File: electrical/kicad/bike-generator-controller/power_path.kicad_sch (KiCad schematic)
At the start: 0 parts

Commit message: feat: build provisional power path schematic
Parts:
- added F1: 20A DC / PROVISOIRE, symbol Device:Fuse
- added F2: F_AUX / PROVISOIRE, symbol Device:Fuse
- added J4: RECTIFIER_IN / PROVISOIRE, symbol Connector_Generic:Conn_01x02
- added J5: BUCK_400W_IN / PROVISOIRE, symbol Connector_Generic:Conn_01x02
- added R7: 2mR 4T / PROVISOIRE, symbol Device:R_Shunt
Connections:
- new net: F1.2, R7.1
- new net: F1.1, J4.1 (Pin_1)
- new net AUX_IN_PROTECTED: F2.2
- new net BUS_PROTECTED: F2.1, J5.1 (Pin_1), R7.4
- new net GND: J4.2 (Pin_2), J5.2 (Pin_2)
- new net SHUNT_HI_K: R7.2
- new net SHUNT_LO_K: R7.3
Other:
- note added: "CHEMIN DE PUISSANCE 400 W - composants mecaniques a confirmer"
- note added: "Depart auxiliaire protege vers LM5164 (10-60 V vers 5 V)"
- note added: "Protection surtension / TVS : A DIMENSIONNER apres mesures generatrice"

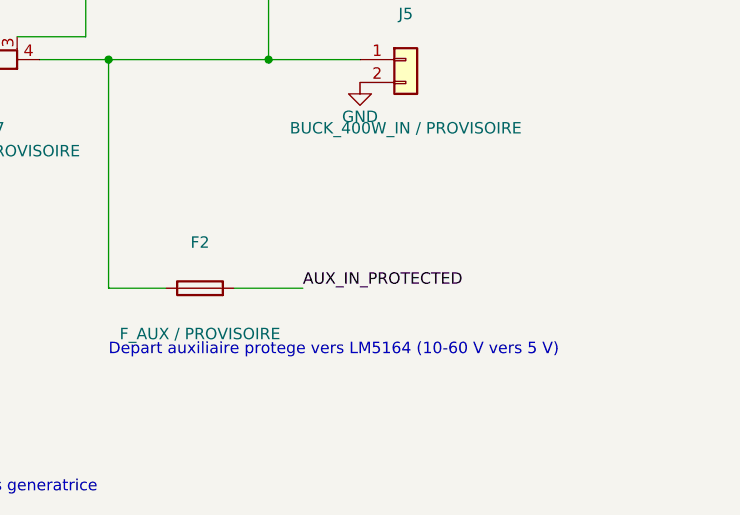
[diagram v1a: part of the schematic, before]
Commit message: feat: add LM5164 auxiliary supply schematic
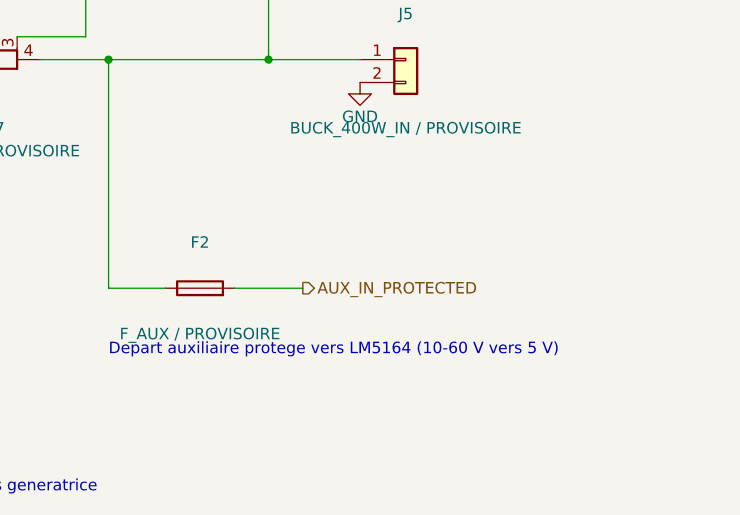
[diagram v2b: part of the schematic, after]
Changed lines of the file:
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@@
-		)
-	)
-	(label "AUX_IN_PROTECTED"
-		(at 143.51 101.6 0)
-		(effects
-			(font
-				(size 1.27 1.27)
-			)
-			(justify left bottom)
 		)
 	)
@@
 		(effects
 			(font
+				(size 1.27 1.27)
+			)
+			(justify left)
+		)
+	)
+	(hierarchical_label "AUX_IN_PROTECTED"
+		(shape output)
+		(at 143.51 101.6 0)
+		(effects
+			(font

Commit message: feat: establish controller PCB V1 design baseline
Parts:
- F1: value 20A DC / PROVISOIRE -> ABC-V-20-R; footprint (none) -> BikeGenerator:Fuse_Eaton_ABC-V-20-R_Axial_P38.10mm; Current Rating (none) -> 20 A; Interrupt Rating (none) -> 10 kA at 125 VDC; MPN (none) -> ABC-V-20-R; Manufacturer (none) -> Eaton Bussmann; Mounting (none) -> Axial THT; Requirement (none) -> Source-specific; 20A maximum; 125VDC minimum; Voltage Rating (none) -> 125 VDC / 250 VAC
- F2: footprint (none) -> BikeGenerator:Fuse_Littelfuse_0449001MR_6.10x2.69mm
- J4: value RECTIFIER_IN / PROVISOIRE -> PHOENIX 1711725 / RECTIFIER_IN; footprint (none) -> TerminalBlock_Phoenix:TerminalBlock_Phoenix_MKDS-3-2-5.08_1x02_P5.08mm_Horizontal; Datasheet Source (none) -> Phoenix Contact official product page; MPN (none) -> 1711725; Manufacturer (none) -> Phoenix Contact; Rated Current (none) -> 24 A; Rated Voltage (none) -> 400 V (III/2); Selection Note (none) -> V1 main-path connector; board path limited to 20 A continuo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; Wire Range (none) -> AWG 24-12 / 0.2-4 mm2 solid
- J5: value BUCK_400W_IN / PROVISOIRE -> PHOENIX 1711725 / BUCK_IN; footprint (none) -> TerminalBlock_Phoenix:TerminalBlock_Phoenix_MKDS-3-2-5.08_1x02_P5.08mm_Horizontal; Datasheet Source (none) -> Phoenix Contact official product page; MPN (none) -> 1711725; Manufacturer (none) -> Phoenix Contact; Rated Current (none) -> 24 A; Rated Voltage (none) -> 400 V (III/2); Selection Note (none) -> V1 main-path connector; board path limited to 20 A continuo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; Wire Range (none) -> AWG 24-12 / 0.2-4 mm2 solid
- R7: value 2mR 4T / PROVISOIRE -> CSS4J-4026K-2L00F 2mR; footprint (none) -> Resistor_SMD:R_Shunt_Isabellenhuette_BVR4026; MPN (none) -> CSS4J-4026K-2L00F; Manufacturer (none) -> Bourns
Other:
- note added: "BUS_PROTECTED : 80 V MAX CONTINU - TVS pour transitoires courts, choix source-specifique"
- note added: "Depart auxiliaire protege vers LM5164 (10-80 V vers 5 V)"
- note removed: "Depart auxiliaire protege vers LM5164 (10-60 V vers 5 V)"
- note removed: "Protection surtension / TVS : A DIMENSIONNER apres mesures generatrice"

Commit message: wip: checkpoint controller routing before review
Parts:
- added D1: SMCJ70A, Diode_SMD:D_SMC, symbol Device:D_Zener
- added D2: DBI25-16A / 3PH BRIDGE, BikeGenerator:Diode_Bridge_Diotec_DBI-A_5Pin_P7.50mm, symbol BikeGenerator:DBI25-16A
- added J8: 3PH_GEN_IN (1=U 2=V 3=W), TerminalBlock_Phoenix:TerminalBlock_Phoenix_MKDS-3-3-5.08_1x03_P5.08mm_Horizontal, symbol Connector_Generic:Conn_01x03
- F1: value ABC-V-20-R -> 0456020.ER / 20A; footprint BikeGenerator:Fuse_Eaton_ABC-V-20-R_Axial_P38.10mm -> BikeGenerator:Fuse_Littelfuse_456_10.08x3.05mm_P9.35mm; Interrupt Rating 10 kA at 125 VDC -> 100 A @125 VAC; 300 A @100 VDC; 500 A @72 VDC; 1000 A @32 V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; MPN ABC-V-20-R -> 0456020.ER; Manufacturer Eaton Bussmann -> Littelfuse; Mounting Axial THT -> SMD; Requirement Source-specific; 20A maximum; 125VDC minimum -> 20 A maximum; voltage and interrupt ratings per Littelfuse 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; Thermal_Management (none) -> Rated-current reference: >=100 um copper and >=10 mm trace 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; Voltage Rating 125 VDC / 250 VAC -> 125 VAC / 100 VDC
- J1: renamed from J4; value PHOENIX 1711725 / RECTIFIER_IN -> DC_GEN_IN / DNP (DC VARIANT); Assembly (none) -> DNP by default - DC generator variant only; Warning (none) -> Respect polarity; never use together with J8
- renumbered J5 to J2, R7 to R1
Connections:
- net BUS_PROTECTED: now also J2.2 (Pin_2), R1.1; no longer J2.1 (Pin_1), R1.4
- net GND: now also J2.1 (Pin_1), D1.2 (A), D2.1 (DC-); no longer J2.2 (Pin_2)
- net SHUNT_HI_K: now also R1.3; no longer R1.2
- net SHUNT_LO_K: now also R1.2; no longer R1.3
- net at F1.2: now also R1.4, D1.1 (K); no longer R1.1
- net RECTIFIED_RAW: now reaches F1.1, J1.1 (Pin_1)
- net RECTIFIED_RAW: now also D2.5 (DC+)
- new net GEN_PHASE_U: D2.4 (AC3), J8.1 (Pin_1)
- new net GEN_PHASE_V: D2.3 (AC2), J8.2 (Pin_2)
- new net GEN_PHASE_W: D2.2 (AC1), J8.3 (Pin_3)
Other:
- note added: "DEFAULT: populate J8 + D2 (3-PHASE INPUT). DC VARIANT: populate J1; D2/J8 may be DNP. ONE INPUT ONLY - NEVER CONNECT J1 AND J8 TO SOURCES AT THE SAME TIME. J1 POLARITY MUST BE RESPECTED."
- note added: "ENTREE GARANTIE <= 70 V CONTINU. SMCJ70A : ecretage transitoire best effort ; INA228 non garantie < 85 V."
- note added: "F1 - THERMIQUE (Littelfuse 0456020.ER) A 20 A : recommandation constructeur >= 100 um Cu et piste >= 10 mm. Si la fabrication differe : valider Tcorps F1 <= 90 degC a Tamb = 25 degC."
- note removed: "BUS_PROTECTED : 80 V MAX CONTINU - TVS pour transitoires courts, choix source-specifique"
- moved on the sheet: F2, J2, R1

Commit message: feat: close controller v1 design and define integrated v2
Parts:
- D2: Thermal Note (none) -> ABOVE 4A USE >=35x25mm ALUMINUM HEATSINK/CHASSIS + TIM + M4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
- F2: value F_AUX / PROVISOIRE -> 0449001.MR / 1A 125V Slo-Blo; MPN (none) -> 0449001.MR; Manufacturer (none) -> Littelfuse
- J1: value DC_GEN_IN / DNP (DC VARIANT) -> DC_GEN_IN / DIRECT DC VARIANT; Assembly DNP by default - DC generator variant only -> Populate on first prototypes - direct DC source variant; Populate (none) -> YES - FIRST PROTOTYPES; Safety Note (none) -> NEVER CONNECT OR ENERGIZE J1 AND J8 AT THE SAME TIME
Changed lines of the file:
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@@
 	(generator_version "10.0")
 	(paper "A4")
+	(text "F1 - THERMIQUE (Littelfuse 0456020.ER)\nA 20 A : recommandation constructeur >= 100 um Cu et piste >= 10 mm.\nSi la fabrication differe : valider Tcorps F1 <= 90 degC a Tamb = 25 degC."
+		(exclude_from_sim no)
+		(at 52.07 109.22 0)
+		(effects
+			(font
+				(size 1 1)
+				(bold yes)
+			)
+			(justify left bottom)
+		)
+	)
 	(text "DEFAULT: populate J8 + D2 (3-PHASE INPUT).\nDC VARIANT: populate J1; D2/J8 may be DNP.\nONE INPUT ONLY - NEVER CONNECT J1 AND J8 TO SOURCES AT THE SAME TIME.\nJ1 POLARITY MUST BE RESPECTED."
 		(exclude_from_sim no)
@@
 		)
 	)
-  (text "F1 - THERMIQUE (Littelfuse 0456020.ER)\nA 20 A : recommandation constructeur >= 100 um Cu et piste >= 10 mm.\nSi la fabrication differe : valider Tcorps F1 <= 90 degC a Tamb = 25 degC."
-    (at 52.07 109.22 0)
-    (effects (font (size 1 1) (bold yes)) (justify left bottom))
-  )
 	(symbol
 		(lib_id "Device:R_Shunt")
@@
 			)
 		)
-		(property "Value" "F_AUX / PROVISOIRE"
+		(property "Value" "0449001.MR / 1A 125V Slo-Blo"
 			(at 132.08 104.14 90)
 			(show_name no)
@@
 			)
 		)
-		(property "Datasheet" ""
+		(property "Datasheet" "https://www.littelfuse.com/assetdocs/fuses-449-datasheet?assetguid=7aef6e93-9808-456e-9bee-fba54271285f"
 			(at 132.08 99.06 0)
 			(hide yes)
@@
 		)
 		(property "Description" "Fuse"
+			(at 132.08 99.06 0)
+			(hide yes)
+			(show_name no)
+			(do_not_autoplace no)
+			(effects
+				(font
+					(size 1.27 1.27)
+				)
+			)
+		)
+		(property "Manufacturer" "Littelfuse"
+			(at 132.08 99.06 0)
+			(hide yes)
+			(show_name no)
+			(do_not_autoplace no)
+			(effects
+				(font
+					(size 1.27 1.27)
+				)
+			)
+		)
+		(property "MPN" "0449001.MR"
 			(at 132.08 99.06 0)
 			(hide yes)
@@
 			)
 		)
+		(property "Thermal Note" "ABOVE 4A USE >=35x25mm ALUMINUM HEATSINK/CHASSIS + TIM + M4; VERIFY TEMPERATURE"
+			(at 81.28 54.61 0)
+			(hide yes)
+			(show_name no)
+			(do_not_autoplace no)
+			(effects
+				(font
+					(size 1.27 1.27)
+				)
+			)
+		)
 		(pin "4"
 		)
@@
 			)
 		)
-		(property "Value" "DC_GEN_IN / DNP (DC VARIANT)"
+		(property "Value" "DC_GEN_IN / DIRECT DC VARIANT"
 			(at 55.88 83.82 0)
 			(show_name no)
@@
 			)
 		)
-		(property "Assembly" "DNP by default - DC generator variant only"
+		(property "Assembly" "Populate on first prototypes - direct DC source variant"
 			(at 55.88 76.2 0)
 			(hide yes)
@@
 		)
 		(property "Warning" "Respect polarity; never use together with J8"
+			(at 55.88 76.2 0)
+			(hide yes)
+			(show_name no)
+			(do_not_autoplace no)
+			(effects
+				(font
+					(size 1.27 1.27)
+				)
+			)
+		)
+		(property "Populate" "YES - FIRST PROTOTYPES"
+			(at 55.88 76.2 0)
+			(hide yes)
+			(show_name no)
+			(do_not_autoplace no)
+			(effects
+				(font
+					(size 1.27 1.27)
+				)
+			)
+		)
+		(property "Safety Note" "NEVER CONNECT OR ENERGIZE J1 AND J8 AT THE SAME TIME"
 			(at 55.88 76.2 0)
 			(hide yes)
@@
 			)
 		)
+		(property "Thermal_Management" "Rated-current reference: >=100 um copper and >=10 mm trace width; otherwise verify fuse body <=90 C at 25 C ambient."
+			(at 81.28 76.2 0)
+			(hide yes)
+			(show_name no)
+			(do_not_autoplace no)
+			(effects
+				(font
+					(size 1.27 1.27)
+				)
+			)
+		)
 		(pin "2"
 		)
@@
 			)
 		)
-		(property "Thermal_Management" "Rated-current reference: >=100 um copper and >=10 mm trace width; otherwise verify fuse body <=90 C at 25 C ambient."
-			(at 81.28 76.2 0)
-			(hide yes)
-			(effects
-				(font
-					(size 1.27 1.27)
-				)
-			)
-		))
+	)
 	(symbol
 		(lib_id "power:GND")

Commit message: feat(pcb): finalize V1 controller layout
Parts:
- R1: footprint Resistor_SMD:R_Shunt_Isabellenhuette_BVR4026 -> BikeGenerator:R_Shunt_Isabellenhuette_BVR4026
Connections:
- net GEN_PHASE_U: now also J8.2 (Pin_2); no longer J8.1 (Pin_1)
- net GEN_PHASE_V: now also J8.3 (Pin_3); no longer J8.2 (Pin_2)
- net GEN_PHASE_W: now also J8.1 (Pin_1); no longer J8.3 (Pin_3)
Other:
- moved on the sheet: J8
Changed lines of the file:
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@@
 	(wire
 		(pts
-			(xy 58.42 57.15) (xy 72.39 57.15)
+			(xy 85.09 76.2) (xy 104.14 76.2)
 		)
 		(stroke
@@
 	(wire
 		(pts
-			(xy 85.09 76.2) (xy 104.14 76.2)
+			(xy 121.92 76.2) (xy 139.7 76.2)
 		)
 		(stroke
@@
 		)
 	)
-	(wire
-		(pts
-			(xy 121.92 76.2) (xy 139.7 76.2)
-		)
-		(stroke
-			(width 0)
-			(type default)
-		)
-	)
-	(wire
-		(pts
-			(xy 58.42 54.61) (xy 72.39 54.61)
-		)
-		(stroke
-			(width 0)
-			(type default)
-		)
-	)
-	(wire
-		(pts
-			(xy 58.42 52.07) (xy 72.39 52.07)
-		)
-		(stroke
-			(width 0)
-			(type default)
+	(label "GEN_PHASE_W"
+		(at 72.39 52.07 180)
+		(effects
+			(font
+				(size 1.27 1.27)
+			)
+			(justify right bottom)
+		)
+	)
+	(label "GEN_PHASE_V"
+		(at 40.64 57.15 0)
+		(effects
+			(font
+				(size 1.27 1.27)
+			)
+			(justify left bottom)
 		)
 	)
@@
 	)
 	(label "GEN_PHASE_U"
-		(at 58.42 57.15 0)
-		(effects
-			(font
-				(size 1.27 1.27)
-			)
-			(justify left bottom)
+		(at 72.39 57.15 180)
+		(effects
+			(font
+				(size 1.27 1.27)
+			)
+			(justify right bottom)
 		)
 	)
 	(label "GEN_PHASE_V"
-		(at 58.42 54.61 0)
+		(at 72.39 54.61 180)
+		(effects
+			(font
+				(size 1.27 1.27)
+			)
+			(justify right bottom)
+		)
+	)
+	(label "GEN_PHASE_W"
+		(at 40.64 52.07 0)
 		(effects
 			(font
@@
 		)
 	)
-	(label "GEN_PHASE_W"
-		(at 58.42 52.07 0)
+	(label "GEN_PHASE_U"
+		(at 40.64 54.61 0)
 		(effects
 			(font
@@
 			)
 		)
-		(property "Footprint" "Resistor_SMD:R_Shunt_Isabellenhuette_BVR4026"
+		(property "Footprint" "BikeGenerator:R_Shunt_Isabellenhuette_BVR4026"
 			(at 109.22 76.2 0)
 			(hide yes)
@@
 	(symbol
 		(lib_id "Connector_Generic:Conn_01x03")
-		(at 53.34 54.61 180)
+		(at 35.56 54.61 0)
+		(mirror y)
 		(unit 1)
 		(body_style 1)
@@
 		(dnp no)
 		(property "Reference" "J8"
-			(at 53.34 59.69 0)
+			(at 35.56 49.53 0)
 			(show_name no)
 			(do_not_autoplace no)
@@
 		)
 		(property "Value" "3PH_GEN_IN (1=U 2=V 3=W)"
-			(at 53.34 49.53 0)
+			(at 14.224 64.008 0)
+			(hide yes)
 			(show_name no)
 			(do_not_autoplace no)
@@
 		)
 		(property "Footprint" "TerminalBlock_Phoenix:TerminalBlock_Phoenix_MKDS-3-3-5.08_1x03_P5.08mm_Horizontal"
-			(at 53.34 54.61 0)
+			(at 35.56 54.61 0)
 			(hide yes)
 			(show_name no)
@@
 		)
 		(property "Datasheet" "https://www.phoenixcontact.com/fr-fr/produits/borne-de-circuit-imprime-mkds-3-3-508-1711738"
-			(at 53.34 54.61 0)
+			(at 35.56 54.61 0)
 			(hide yes)
 			(show_name no)
@@
 		)
 		(property "Description" "Generic connector, single row, 01x03, script generated (kicad-library-utils/schlib/autogen/connector/)"
-			(at 53.34 54.61 0)
+			(at 35.56 54.61 0)
 			(hide yes)
 			(show_name no)
@@
 		)
 		(property "Assembly" "Populate by default - 3-phase variant"
-			(at 53.34 54.61 0)
+			(at 35.56 54.61 0)
 			(hide yes)
 			(show_name no)
@@
 		)
 		(property "Warning" "Never use together with J1"
-			(at 53.34 54.61 0)
+			(at 35.56 54.61 0)
 			(hide yes)
 			(show_name no)
@@
 		)
 		(property "Datasheet Source" "Phoenix Contact official product page"
-			(at 53.34 54.61 0)
+			(at 35.56 54.61 0)
 			(hide yes)
 			(show_name no)
@@
 		)
 		(property "MPN" "1711738"
-			(at 53.34 54.61 0)
+			(at 35.56 54.61 0)
 			(hide yes)
 			(show_name no)
@@
 		)
 		(property "Manufacturer" "Phoenix Contact"
-			(at 53.34 54.61 0)
+			(at 35.56 54.61 0)
 			(hide yes)
 			(show_name no)
@@
 		)
 		(property "Rated Current" "24 A"
-			(at 53.34 54.61 0)
+			(at 35.56 54.61 0)
 			(hide yes)
 			(show_name no)
@@
 		)
 		(property "Rated Voltage" "400 V (III/2)"
-			(at 53.34 54.61 0)
+			(at 35.56 54.61 0)
 			(hide yes)
 			(show_name no)
@@
 		)
 		(property "Wire Range" "2.5 mm2 nominal"
-			(at 53.34 54.61 0)
-			(hide yes)
-			(show_name no)
+			(at 35.56 54.61 0)
+			(hide yes)
+			(show_name no)
